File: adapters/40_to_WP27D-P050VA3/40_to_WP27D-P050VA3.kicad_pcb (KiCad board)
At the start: 2 copper layers, 40 x 30 mm, 3 parts, among them CN1 WP27D-S050VA3-R15000, J1 Conn_01x05_Pin, U1 ED078KH6

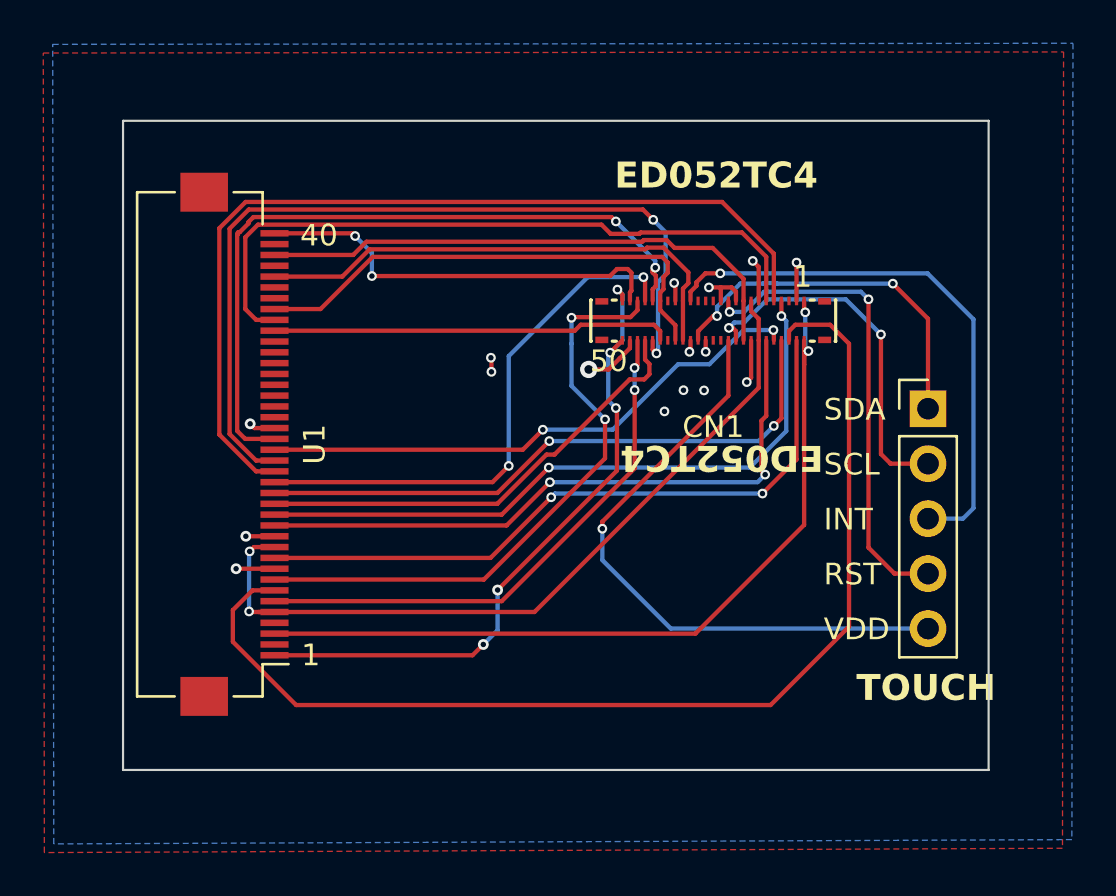
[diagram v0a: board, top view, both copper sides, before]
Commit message: Fix adapter with correct pinout
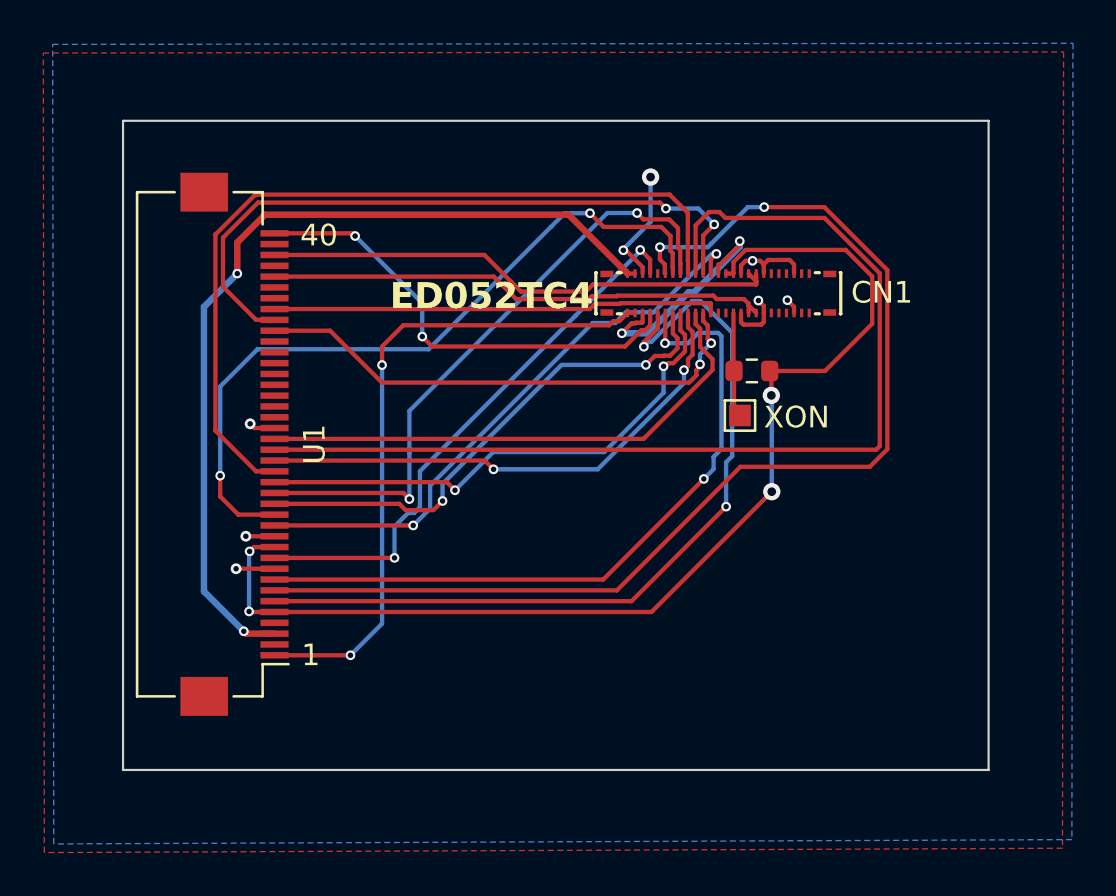
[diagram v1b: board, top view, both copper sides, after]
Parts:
- removed J1: Conn_01x05_Pin, Connector_PinHeader_2.54mm:PinHeader_1x05_P2.54mm_Vertical
- added R1: 10K, Resistor_SMD:R_0603_1608Metric, F.Cu at (43.1, 20.6)
- added TP1: XON, TestPoint:TestPoint_Pad_1.0x1.0mm, F.Cu at (42.6, 22.6)
- moved CN1 1.29 mm to (41.6, 17.0), turned to 0 degrees
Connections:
- CN1 pad 20: TP_SCL -> unconnected-(CN1-Pad20)
- CN1 pad 21: TP_RST -> unconnected-(CN1-Pad21)
- CN1 pad 22: TP_VDD -> unconnected-(CN1-Pad22)
- CN1 pad 30: TP_SDA -> unconnected-(CN1-Pad30)
- CN1 pad 31: TP_INT -> unconnected-(CN1-Pad31)
- CN1 pad 36: /XOE -> Net-(CN1-Pad36)
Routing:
- net TP_VDD: track 28.9 -> 0.00 mm, vias 1 -> 0
- net TP_INT: track 25.9 -> 0.00 mm, vias 1 -> 0
- net /D6: track 25.8 -> 48.2 mm, vias 2 -> 0
- net TP_RST: track 22.2 -> 0.00 mm, vias 2 -> 0
- net TP_SDA: track 17.1 -> 0.00 mm, vias 2 -> 0
- net TP_SCL: track 16.9 -> 0.00 mm, vias 2 -> 0
- net VDD: track 36.8 -> 52.7 mm, vias 2 -> 4
- net /D5: track 39.5 -> 24.2 mm
- net /MODE: track 25.2 -> 38.2 mm
- net GND: track 17.7 -> 28.0 mm, vias 16 -> 10
- net /D7: track 33.5 -> 24.5 mm, vias 2 -> 0
- net /VCOM: track 31.5 -> 25.9 mm
- net /XSTL: track 18.5 -> 23.9 mm, vias 0 -> 2
- net Net-(CN1-Pad36): track 0.00 -> 4.86 mm
- net /SPV: track 28.4 -> 33.0 mm
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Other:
- board text added: "XON"
- board text removed: "50"
- board text removed: "INT"
- board text removed: "RST"
- board text removed: "SCL"
- board text removed: "SDA"
- board text removed: "TOUCH"
- board text removed: "VDD"

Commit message: Update ED052TC4 Adapter with right positioning
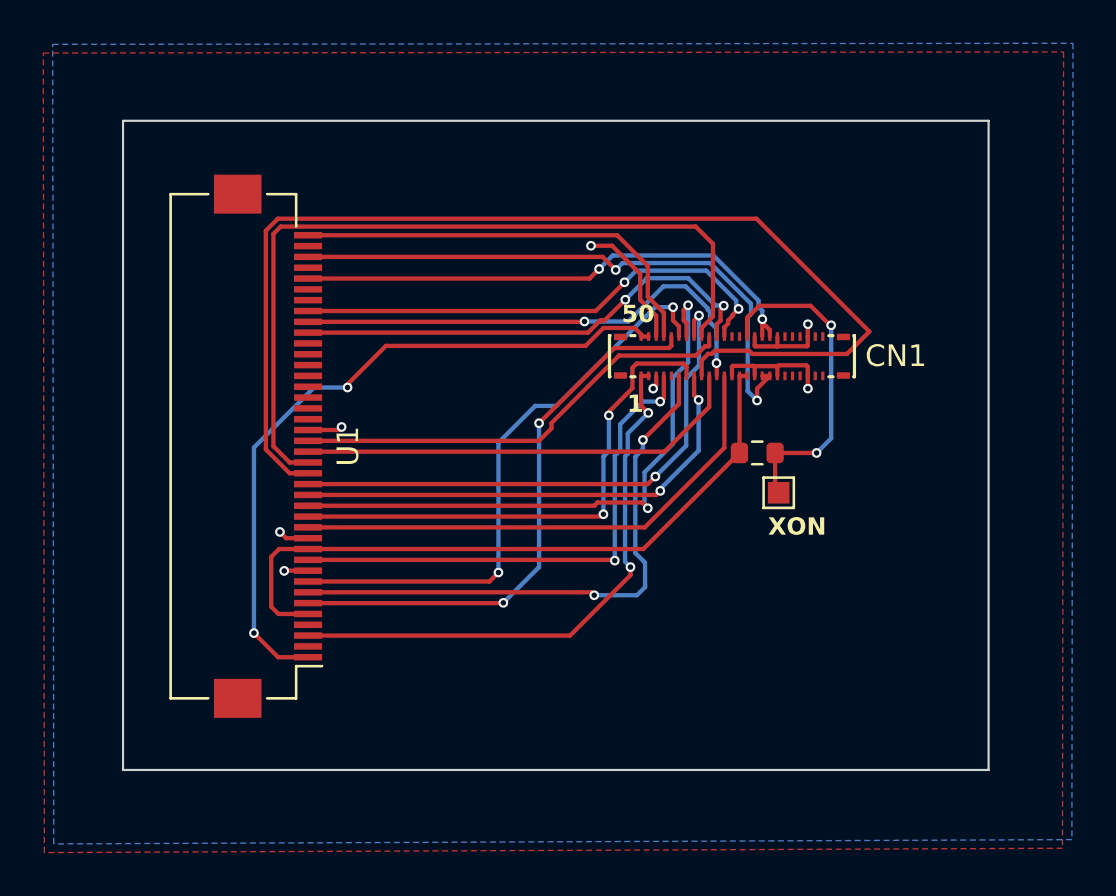
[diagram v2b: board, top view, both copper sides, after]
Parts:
- moved TP1 3.99 mm to (44.4, 26.2)
- moved R1 3.80 mm to (43.4, 24.4), turned to 180 degrees
- moved CN1 2.98 mm to (42.2, 19.9)
- moved U1 1.55 mm to (20.8, 24.0)
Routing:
- net /D6: track 48.2 -> 20.8 mm
- net /CKV: track 53.1 -> 26.6 mm
- net VDD: track 52.7 -> 31.7 mm, vias 4 -> 0
- net /VGH: track 40.9 -> 26.3 mm
- net /D4: track 38.3 -> 51.9 mm
- net /D5: track 24.2 -> 37.0 mm, vias 2 -> 0
- net /MODE: track 38.2 -> 26.0 mm
- net Net-(CN1-Pad36): track 4.86 -> 15.4 mm, vias 0 -> 2
- net /D0: track 34.3 -> 24.1 mm
- net /XLE: track 31.6 -> 22.9 mm
- net GND: track 28.0 -> 21.0 mm, vias 10 -> 7
- net /D2: track 29.1 -> 22.5 mm
- net /SPV: track 33.0 -> 27.1 mm
- net /VNEG: track 24.2 -> 28.1 mm, vias 0 -> 2
- net /D1: track 24.0 -> 27.7 mm
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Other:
- board text added: "50"
- board text removed: "40"
- board text removed: "ED052TC4"
